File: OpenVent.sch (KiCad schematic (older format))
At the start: 0 parts

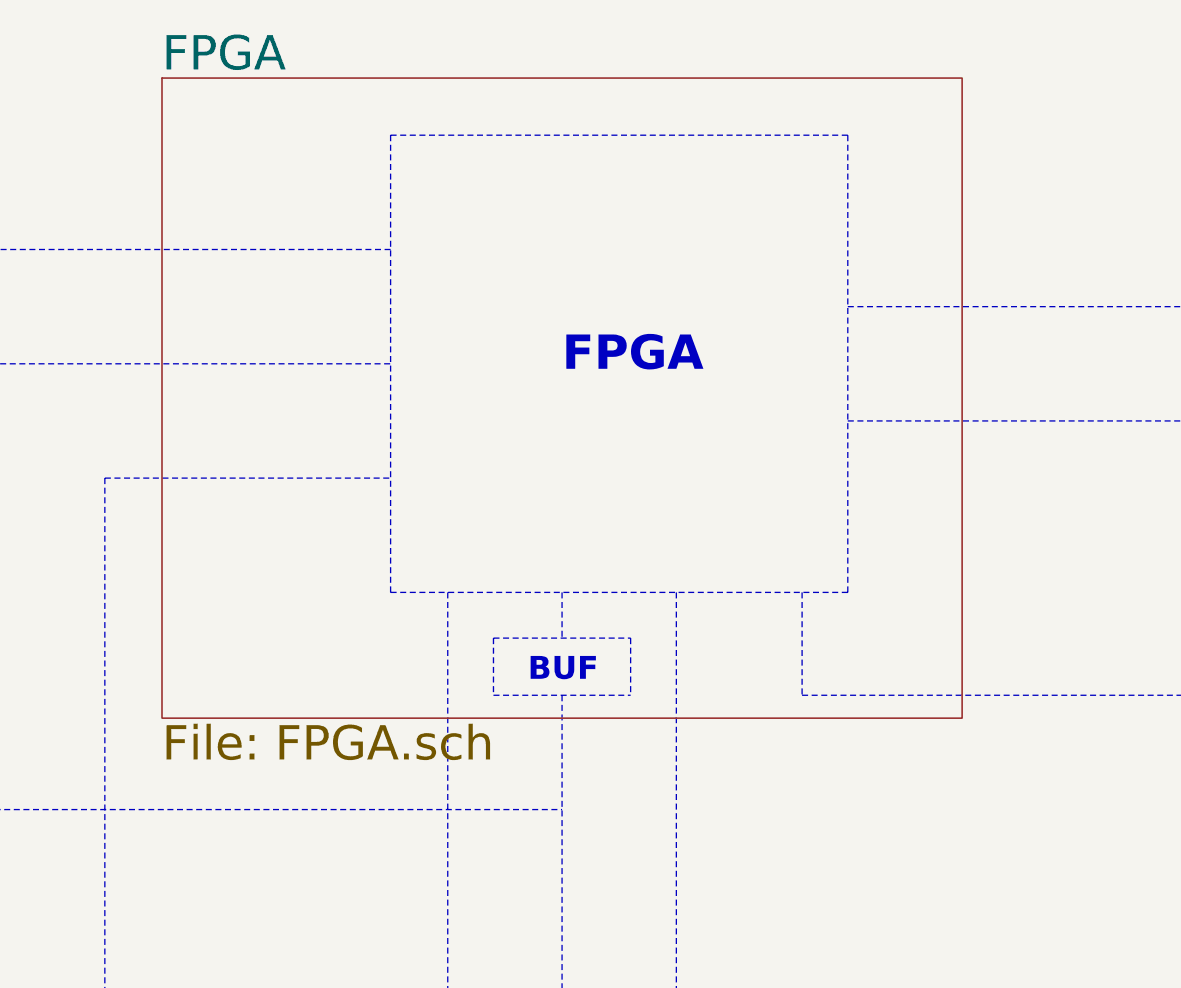
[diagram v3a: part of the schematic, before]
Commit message: Updated the project to include a M2GL010-1TQG144 IGLOO2 FPGA instead of the GOWIN. Since the IGLOO has some 2.5V BANKs as well as 3.3V Banks, some circuitry will need to be modified elsewhere in the circuit, but most of the interfaces are easily changeable, be it different power supplies or the additions of transistors or potential dividers. I will edit the rest of the design later, and write up a list of things I changed for the other peeps in the design team to review
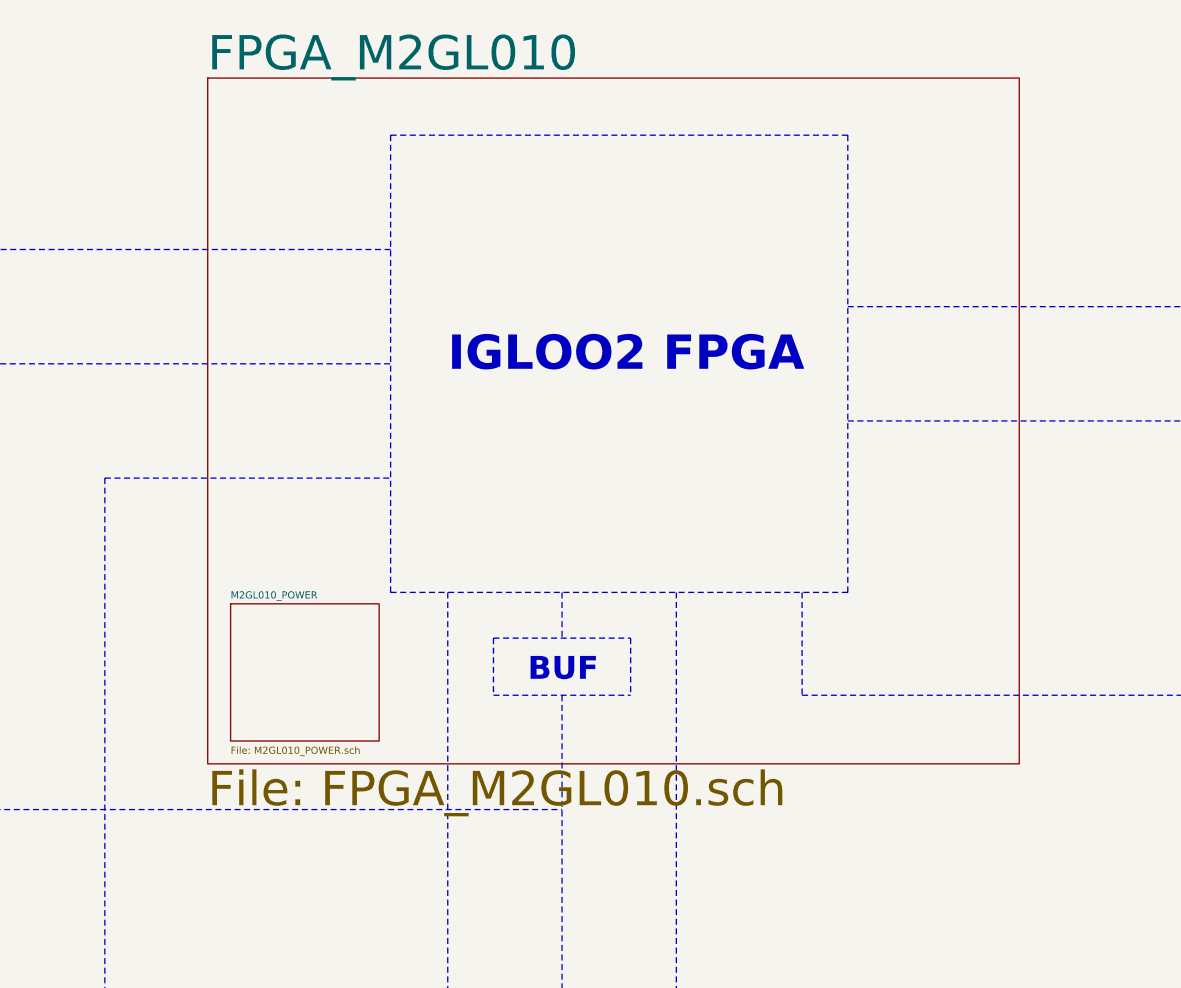
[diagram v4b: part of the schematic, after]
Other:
- note added: "IGLOO2 FPGA"
- note removed: "FPGA"
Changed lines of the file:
@@
 EESchema Schematic File Version 4
-EELAYER 30 0
+LIBS:OpenVent-cache
+EELAYER 26 0
 EELAYER END
 $Descr A3 16535 11693
 encoding utf-8
-Sheet 1 8
+Sheet 1 9
 Title "OpenVent Control Board"
 Date "2020-10-20"
@@
 Wire Notes Line width 20 style solid
 	7000 1250 9000 1250
-Text Notes 7750 2300 0    150  ~ 30
-FPGA
+Text Notes 7250 2300 0    150  ~ 30
+IGLOO2 FPGA
 Wire Notes Line width 12 style solid
 	8250 3250 8250 7700
@@
 F0 "UI" 150
 F1 "UI.sch" 150
-$EndSheet
-$Sheet
-S 6000 1000 3500 2800
-U 5F8F894A
-F0 "FPGA" 150
-F1 "FPGA.sch" 150
 $EndSheet
 $Sheet
@@
 Text Notes 12300 9450 0    120  ~ 24
 nRST
+$Sheet
+S 6200 1000 3550 3000
+U 61A33A68
+F0 "FPGA_M2GL010" 150
+F1 "FPGA_M2GL010.sch" 150
+$EndSheet
+$Sheet
+S 6300 3300 650  600
+U 61A795A0
+F0 "M2GL010_POWER" 31
+F1 "M2GL010_POWER.sch" 31
+$EndSheet
 $EndSCHEMATC

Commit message: Does this actually work, Git?
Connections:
- wire segments 0 -> 1
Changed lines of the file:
@@
 F1 "M2GL010_POWER.sch" 31
 $EndSheet
+Wire Wire Line
+	10200 6100 11300 6100
 $EndSCHEMATC

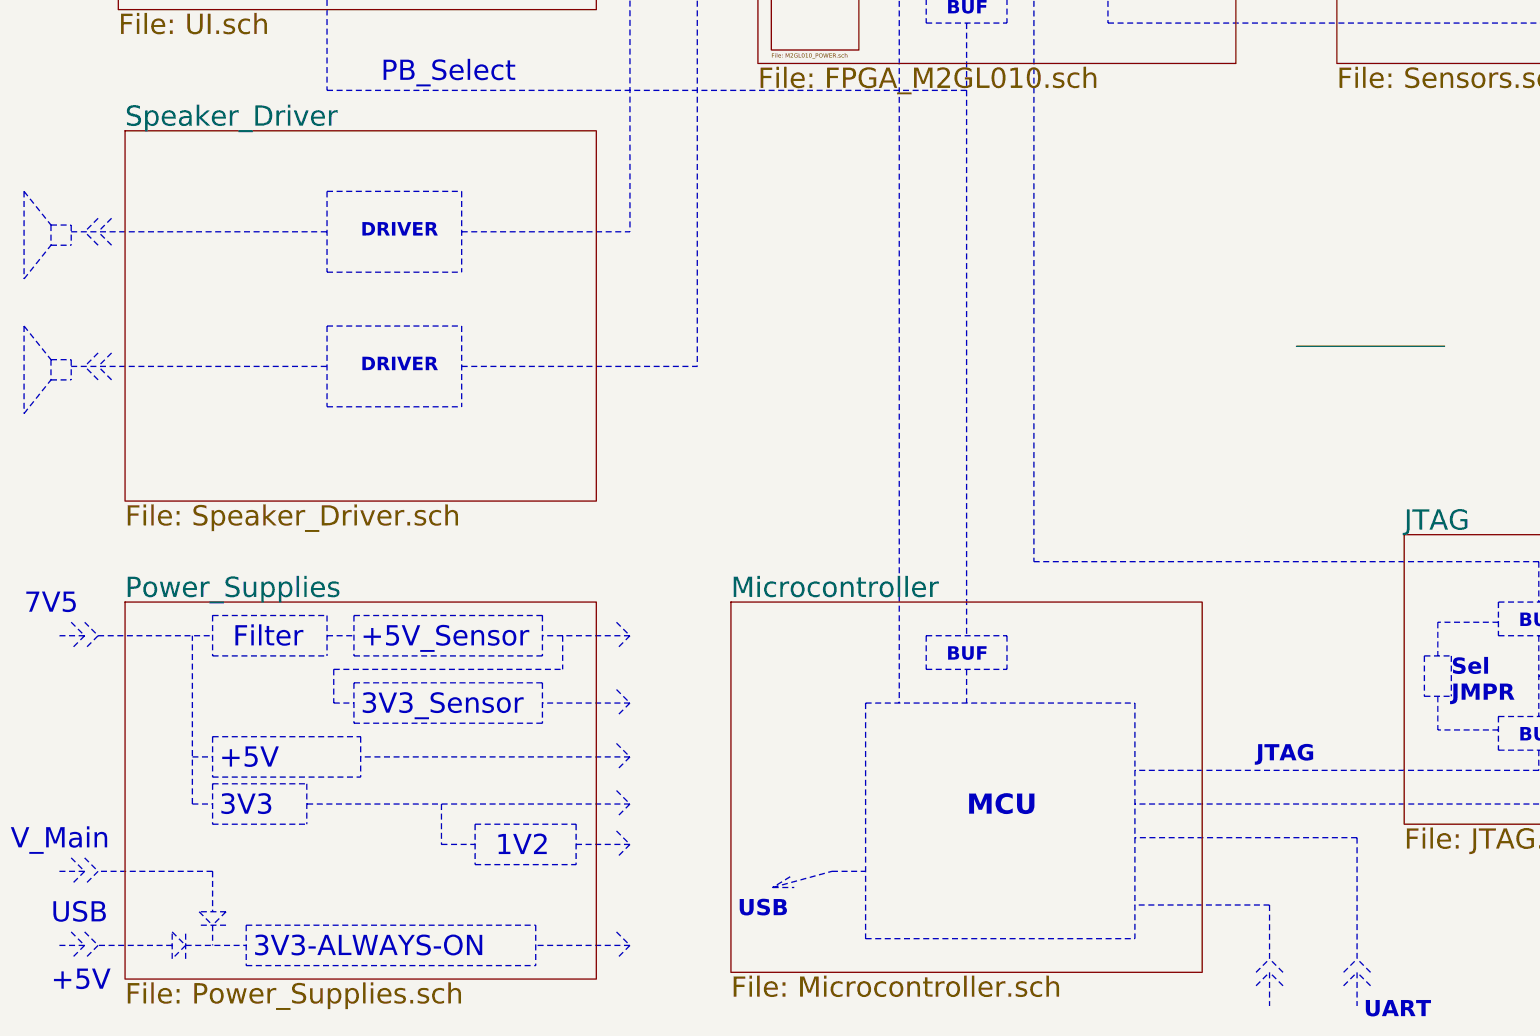
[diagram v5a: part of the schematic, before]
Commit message: Finalised most of the schematic. I think there are a few more things to do in the Speaker
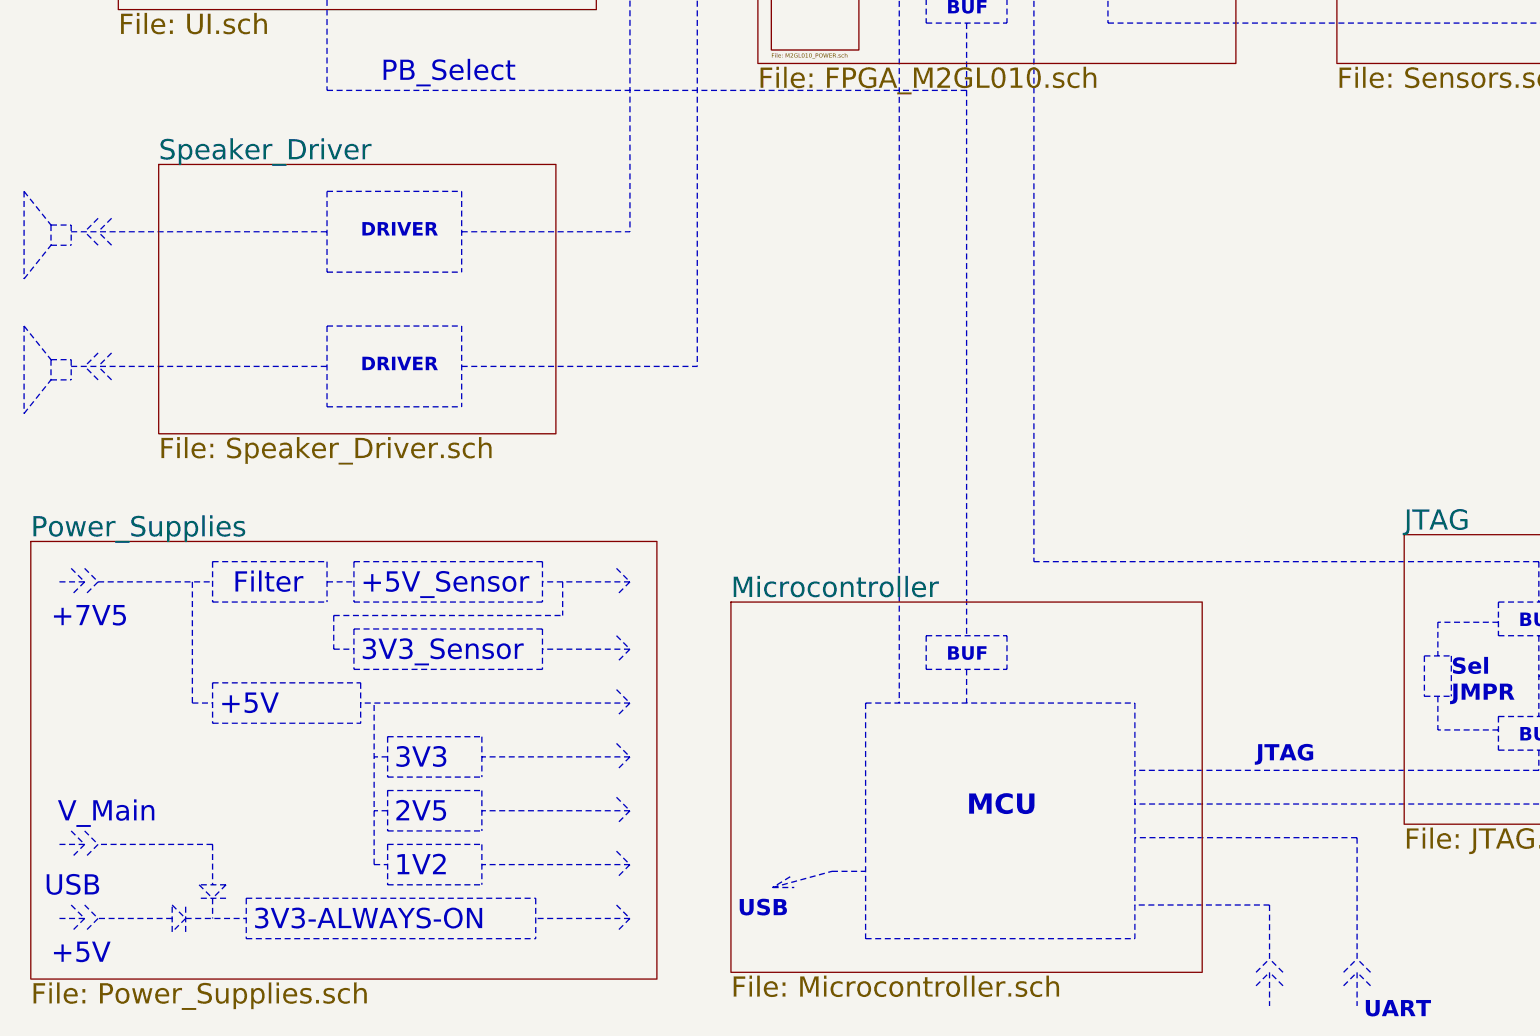
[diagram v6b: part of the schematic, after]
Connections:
- wire segments 1 -> 0
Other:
- note added: "+7V5"
- note added: "2V5"
- note removed: "7V5"
